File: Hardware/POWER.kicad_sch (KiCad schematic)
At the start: 0 parts

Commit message: Checkpoint
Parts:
- added BT1: Battery_Cell, symbol Device:Battery_Cell
- added U5, U7: AP2112K-3.3, Package_TO_SOT_SMD:SOT-23-5, symbol Regulator_Linear:AP2112K-3.3
- added U6: AP2112K-1.8, Package_TO_SOT_SMD:SOT-23-5, symbol Regulator_Linear:AP2112K-1.8
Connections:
- new net: U5.1 (VIN), U5.3 (EN)
- new net D0_3V3_BACKUP: BT1.1 (+)
- new net D1_3V3: U5.5 (VOUT)
- new net D2_1V8: U6.5 (VOUT)
- new net D2_3V3: U7.5 (VOUT)
- new net GND: BT1.2 (-)
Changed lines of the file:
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@@
 (kicad_sch (version 20230121) (generator eeschema)
   (paper "A4")
+  (wire (pts (xy 50.8 38.1) (xy 53.34 38.1))
+    (stroke (width 0) (type default))
+  )
+  (wire (pts (xy 30.48 170.18) (xy 30.48 172.72))
+    (stroke (width 0) (type default))
+  )
+  (wire (pts (xy 50.8 40.64) (xy 50.8 38.1))
+    (stroke (width 0) (type default))
+  )
+  (wire (pts (xy 53.34 40.64) (xy 50.8 40.64))
+    (stroke (width 0) (type default))
+  )
+  (wire (pts (xy 33.02 170.18) (xy 30.48 170.18))
+    (stroke (width 0) (type default))
+  )
+  (bus (pts (xy 241.3 25.4) (xy 266.7 25.4))
+    (stroke (width 0) (type default))
+  )
+  (label "MEAS_S[1..6]" (at 241.3 25.4 0) (fields_autoplaced)
+    (effects (font (size 1.27 1.27)) (justify left bottom))
+  )
+  (hierarchical_label "SERVO_5V5" (shape input) (at 127 116.84 0) (fields_autoplaced)
+    (effects (font (size 1.27 1.27)) (justify left))
+  )
+  (hierarchical_label "D1_5V" (shape passive) (at 127 104.14 0) (fields_autoplaced)
+    (effects (font (size 1.27 1.27)) (justify left))
+  )
+  (hierarchical_label "D1_3V3" (shape passive) (at 68.58 38.1 0) (fields_autoplaced)
+    (effects (font (size 1.27 1.27)) (justify left))
+  )
+  (hierarchical_label "D2_3V3" (shape passive) (at 170.18 63.5 0) (fields_autoplaced)
+    (effects (font (size 1.27 1.27)) (justify left))
+  )
+  (hierarchical_label "MEAS_S[1..6]" (shape output) (at 266.7 25.4 0) (fields_autoplaced)
+    (effects (font (size 1.27 1.27)) (justify left))
+  )
+  (hierarchical_label "D2_EN" (shape input) (at 152.4 109.22 0) (fields_autoplaced)
+    (effects (font (size 1.27 1.27)) (justify left))
+  )
+  (hierarchical_label "D2_1V8" (shape passive) (at 170.18 33.02 0) (fields_autoplaced)
+    (effects (font (size 1.27 1.27)) (justify left))
+  )
+  (hierarchical_label "D1_EN" (shape input) (at 152.4 106.68 0) (fields_autoplaced)
+    (effects (font (size 1.27 1.27)) (justify left))
+  )
+  (hierarchical_label "MEAS_SERVO" (shape output) (at 152.4 114.3 0) (fields_autoplaced)
+    (effects (font (size 1.27 1.27)) (justify left))
+  )
+  (hierarchical_label "D0_3V3_BACKUP" (shape passive) (at 33.02 170.18 0) (fields_autoplaced)
+    (effects (font (size 1.27 1.27)) (justify left))
+  )
+  (symbol (lib_id "Regulator_Linear:AP2112K-3.3") (at 60.96 40.64 0) (unit 1)
+    (in_bom yes) (on_board yes) (dnp no) (fields_autoplaced)
+    (property "Reference" "U5" (at 60.96 31.75 0)
+      (effects (font (size 1.27 1.27)))
+    )
+    (property "Value" "AP2112K-3.3" (at 60.96 34.29 0)
+      (effects (font (size 1.27 1.27)))
+    )
+    (property "Footprint" "Package_TO_SOT_SMD:SOT-23-5" (at 60.96 32.385 0)
+      (effects (font (size 1.27 1.27)) hide)
+    )
+    (property "Datasheet" "https://www.diodes.com/assets/Datasheets/AP2112.pdf" (at 60.96 38.1 0)
+      (effects (font (size 1.27 1.27)) hide)
+    )
+    (pin "1")
+    (pin "2")
+    (pin "3")
+    (pin "4")
+    (pin "5")
+    (instances
+      (project "Avionus_Flight_Controller"
+        (path "/ddc7e940-0588-4587-8902-8ced9e615ace/26f6db01-be5b-4944-aca8-25d2b5bac430"
+          (reference "U5") (unit 1)
+        )
+      )
+    )
+  )
+  (symbol (lib_id "power:GND") (at 30.48 180.34 0) (unit 1)
+    (in_bom yes) (on_board yes) (dnp no) (fields_autoplaced)
+    (property "Reference" "#PWR012" (at 30.48 186.69 0)
+      (effects (font (size 1.27 1.27)) hide)
+    )
+    (property "Value" "GND" (at 30.48 185.42 0)
+      (effects (font (size 1.27 1.27)))
+    )
+    (property "Footprint" "" (at 30.48 180.34 0)
+      (effects (font (size 1.27 1.27)) hide)
+    )
+    (property "Datasheet" "" (at 30.48 180.34 0)
+      (effects (font (size 1.27 1.27)) hide)
+    )
+    (pin "1")
+    (instances
+      (project "Avionus_Flight_Controller"
+        (path "/ddc7e940-0588-4587-8902-8ced9e615ace/26f6db01-be5b-4944-aca8-25d2b5bac430"
+          (reference "#PWR012") (unit 1)
+        )
+      )
+    )
+  )
+  (symbol (lib_id "Regulator_Linear:AP2112K-3.3") (at 162.56 66.04 0) (unit 1)
+    (in_bom yes) (on_board yes) (dnp no) (fields_autoplaced)
+    (property "Reference" "U7" (at 162.56 57.15 0)
+      (effects (font (size 1.27 1.27)))
+    )
+    (property "Value" "AP2112K-3.3" (at 162.56 59.69 0)
+      (effects (font (size 1.27 1.27)))
+    )
+    (property "Footprint" "Package_TO_SOT_SMD:SOT-23-5" (at 162.56 57.785 0)
+      (effects (font (size 1.27 1.27)) hide)
+    )
+    (property "Datasheet" "https://www.diodes.com/assets/Datasheets/AP2112.pdf" (at 162.56 63.5 0)
+      (effects (font (size 1.27 1.27)) hide)
+    )
+    (pin "1")
+    (pin "2")
+    (pin "3")
+    (pin "4")
+    (pin "5")
+    (instances
+      (project "Avionus_Flight_Controller"
+        (path "/ddc7e940-0588-4587-8902-8ced9e615ace/26f6db01-be5b-4944-aca8-25d2b5bac430"
+          (reference "U7") (unit 1)
+        )
+      )
+    )
+  )
+  (symbol (lib_id "Regulator_Linear:AP2112K-1.8") (at 162.56 35.56 0) (unit 1)
+    (in_bom yes) (on_board yes) (dnp no) (fields_autoplaced)
+    (property "Reference" "U6" (at 162.56 26.67 0)
+      (effects (font (size 1.27 1.27)))
+    )
+    (property "Value" "AP2112K-1.8" (at 162.56 29.21 0)
+      (effects (font (size 1.27 1.27)))
+    )
+    (property "Footprint" "Package_TO_SOT_SMD:SOT-23-5" (at 162.56 27.305 0)
+      (effects (font (size 1.27 1.27)) hide)
+    )
+    (property "Datasheet" "https://www.diodes.com/assets/Datasheets/AP2112.pdf" (at 162.56 33.02 0)
+      (effects (font (size 1.27 1.27)) hide)
+    )
+    (pin "1")
+    (pin "2")
+    (pin "3")
+    (pin "4")
+    (pin "5")
+    (instances
+      (project "Avionus_Flight_Controller"
+        (path "/ddc7e940-0588-4587-8902-8ced9e615ace/26f6db01-be5b-4944-aca8-25d2b5bac430"
+          (reference "U6") (unit 1)
+        )
+      )
+    )
+  )
+  (symbol (lib_id "Device:Battery_Cell") (at 30.48 177.8 0) (unit 1)
+    (in_bom yes) (on_board yes) (dnp no) (fields_autoplaced)
+    (property "Reference" "BT1" (at 34.29 174.6885 0)
+      (effects (font (size 1.27 1.27)) (justify left))
+    )
+    (property "Value" "Battery_Cell" (at 34.29 177.2285 0)
+      (effects (font (size 1.27 1.27)) (justify left))
+    )
+    (property "Footprint" "" (at 30.48 176.276 90)
+      (effects (font (size 1.27 1.27)) hide)
+    )
+    (property "Datasheet" "~" (at 30.48 176.276 90)
+      (effects (font (size 1.27 1.27)) hide)
+    )
+    (pin "1")
+    (pin "2")
+    (instances
+      (project "Avionus_Flight_Controller"
+        (path "/ddc7e940-0588-4587-8902-8ced9e615ace/26f6db01-be5b-4944-aca8-25d2b5bac430"
+          (reference "BT1") (unit 1)
+        )
+      )
+    )
+  )
 )

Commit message: Checkpoint
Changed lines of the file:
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@@
+    (effects (font (size 1.27 1.27)) (justify left))
+  )
+  (hierarchical_label "USB_5V" (shape input) (at 127 119.38 0) (fields_autoplaced)
     (effects (font (size 1.27 1.27)) (justify left))
   )

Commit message: Checkpoint
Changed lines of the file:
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@@
+    (effects (font (size 1.27 1.27)) (justify left))
+  )
+  (hierarchical_label "POWER_LED_EN" (shape input) (at 152.4 116.84 0) (fields_autoplaced)
     (effects (font (size 1.27 1.27)) (justify left))
   )

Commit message: Checkpoint
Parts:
- added C13, C14, C15, C16, C17, C18: 1uF, symbol Device:C_Small
- added C15: 120uF, Capacitor_THT:C_Radial_D6.3mm_H11.0mm_P2.50mm, symbol Device:C
- added C19, C20, C21, C22: 100nF, symbol Device:C_Small
- added C30, C39: 22uF, Capacitor_SMD:C_1210_3225Metric, symbol Device:C
- added C31: 1uF, Capacitor_SMD:C_0805_2012Metric, symbol Device:C
- added C33: 100pF, Capacitor_SMD:C_0805_2012Metric, symbol Device:C
- added C34: 100nF, Capacitor_SMD:C_0805_2012Metric, symbol Device:C
- added D1, D2, D3: ~, symbol Device:LED_Small
- added D13: B540C-13-F, Diode_SMD:D_SMC, symbol Device:D_Schottky
- added F1: 2000mA, Fuse:Fuse_1206_3216Metric, symbol Device:Polyfuse
- added J15: 5V_USB, symbol Connector_Generic:Conn_01x02
- added J17: Battery IN, symbol Connector_Generic:Conn_01x07
- added L1: SRP6530A-6R8M, leptunKicadLib:SRP6530A-6R8M, symbol Device:L
- added Q1: RE1C002UN, Package_TO_SOT_SMD:SOT-416, symbol Device:Q_NMOS_GSD
- added R25: 15K, Resistor_SMD:R_1206_3216Metric, symbol Device:R
- added R28: 52.3K, Resistor_SMD:R_1206_3216Metric, symbol Device:R_Small
- added R29: 10K, Resistor_SMD:R_1206_3216Metric, symbol Device:R_Small
- added R32: 100, symbol Device:R_Small
- added R33, R40, R41, R42, R46, R47, R48, R49, R50, R51, R52: 100K, symbol Device:R_Small
- added R34, R38, R39: 1K, symbol Device:R_Small
- added R53, R54, R55, R56, R57, R58, R59: 10K, symbol Device:R_Small
- added TP2, TP3, TP4, TP5, TP6, TP7: ~, symbol Connector:TestPoint
- added U11: AOZ1212AI, leptunKicadLib:AOZ1212AI, symbol leptunKicadLib:AOZ1212AI
- added U5 (x2): AP2151W, Package_TO_SOT_SMD:SOT-23-5, symbol leptunKicadLib:AP2151W
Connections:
- net D0_3V3_BACKUP: now also TP2.1
- net D1_3V3: now also C14.1
- net D1_5V: now also U5.1 (VIN), U5.3 (EN), U6.1 (VIN), U7.1 (VIN), C13.1, C15.1, C17.1, C19.1, C20.1, C39.2, J15.2 (Pin_2), L1.2, R28.1, TP3.1, U5.5 (IN), U5.5 (IN)
- net D1_EN: now also R34.1, R40.2, U11.6 (EN)
- net D2_1V8: now also C16.1, TP5.1
- net D2_3V3: now also C18.1, TP4.1
- net D2_EN: now also U6.3 (EN), U7.3 (EN), R38.1, R41.1
- net GND: now also U5.2 (GND), U6.2 (GND), U7.2 (GND), C13.2, C14.2, C15.2, C15.2, C16.2, C17.2, C18.2, C19.2, C20.2, C21.2, C22.2, C30.1, C31.1, C33.1, C39.1, D13.2 (A), J17.1 (Pin_1), Q1.2 (S), R29.2, R33.2, R40.1, R41.2, R42.2, R53.2, R54.2, R55.2, R56.2, R57.2, R58.2, R59.2, U11.3 (GND), U5.2 (GND), U5.2 (GND)
- net MEAS_SERVO: now also R52.2, R53.1
- net SERVO_5V5: now also C15.1, C21.1, C22.1, R52.1, TP7.1, U5.1 (OUT), U5.1 (OUT)
- net USB_5V: now also J15.1 (Pin_1), TP6.1
- new net: D1.1 (K), D2.1 (K), D3.1 (K), Q1.3 (D)
- new net: D3.2 (A), R39.2
- new net: Q1.1 (G), R32.2
- new net: D2.2 (A), R38.2
- new net: C33.2, R25.1
- new net: R25.2, U11.5 (COMP)
- new net: R28.2, R29.1, U11.4 (FB)
- new net: D1.2 (A), R34.2
- new net: C31.2, U11.8 (VBIAS)
- new net: C34.2, D13.1 (K), L1.1, U11.1 (LX)
- new net: C34.1, U11.2 (BST)
- new net: C30.2, F1.1, U11.7 (VIN)
- new net BATT_S1: J17.2 (Pin_2), R51.2
- new net BATT_S2: J17.3 (Pin_3), R50.1
- new net BATT_S3: J17.4 (Pin_4), R49.1
- new net BATT_S4: J17.5 (Pin_5), R48.1
- new net BATT_S5: J17.6 (Pin_6), R47.1
- new net BATT_S6: F1.2, J17.7 (Pin_7), R46.1
- new net LEDs_EN: R32.1, R33.1
- new net MEAS_S1: R51.1, R59.1
- new net MEAS_S2: R50.2, R58.1
- new net MEAS_S3: R49.2, R57.1
- new net MEAS_S4: R48.2, R56.1
- new net MEAS_S5: R47.2, R55.1
- new net MEAS_S6: R46.2, R54.1
- new net SERVO_5V_AUX_EN: R39.1, R42.1, U5.4 (EN), U5.4 (EN)
- new net SERVO_5V_AUX_FAULT: U5.3 (~{FLG}), U5.3 (~{FLG})
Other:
- moved on the sheet: BT1, U5, U6, U7

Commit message: Checkpoint
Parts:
- added C48: 4.7uF, symbol Device:C_Small
- added D5: BAT54C, Package_TO_SOT_SMD:SOT-23, symbol Diode:BAT54C
- C33, C34: footprint Capacitor_SMD:C_0805_2012Metric -> (none)
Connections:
- net D1_EN: now also D5.1; no longer R40.2, U11.6 (EN)
- net GND: now also R40.2, C48.2; no longer R40.1
- net at C30.2, F1.1, U11.7 (VIN): now also D5.2
- new net: C48.1, D5.3, R40.1, U11.6 (EN)
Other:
- moved on the sheet: C30, C31, C33, C34, C39, D13, F1, L1, R25, R28, R29, R40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

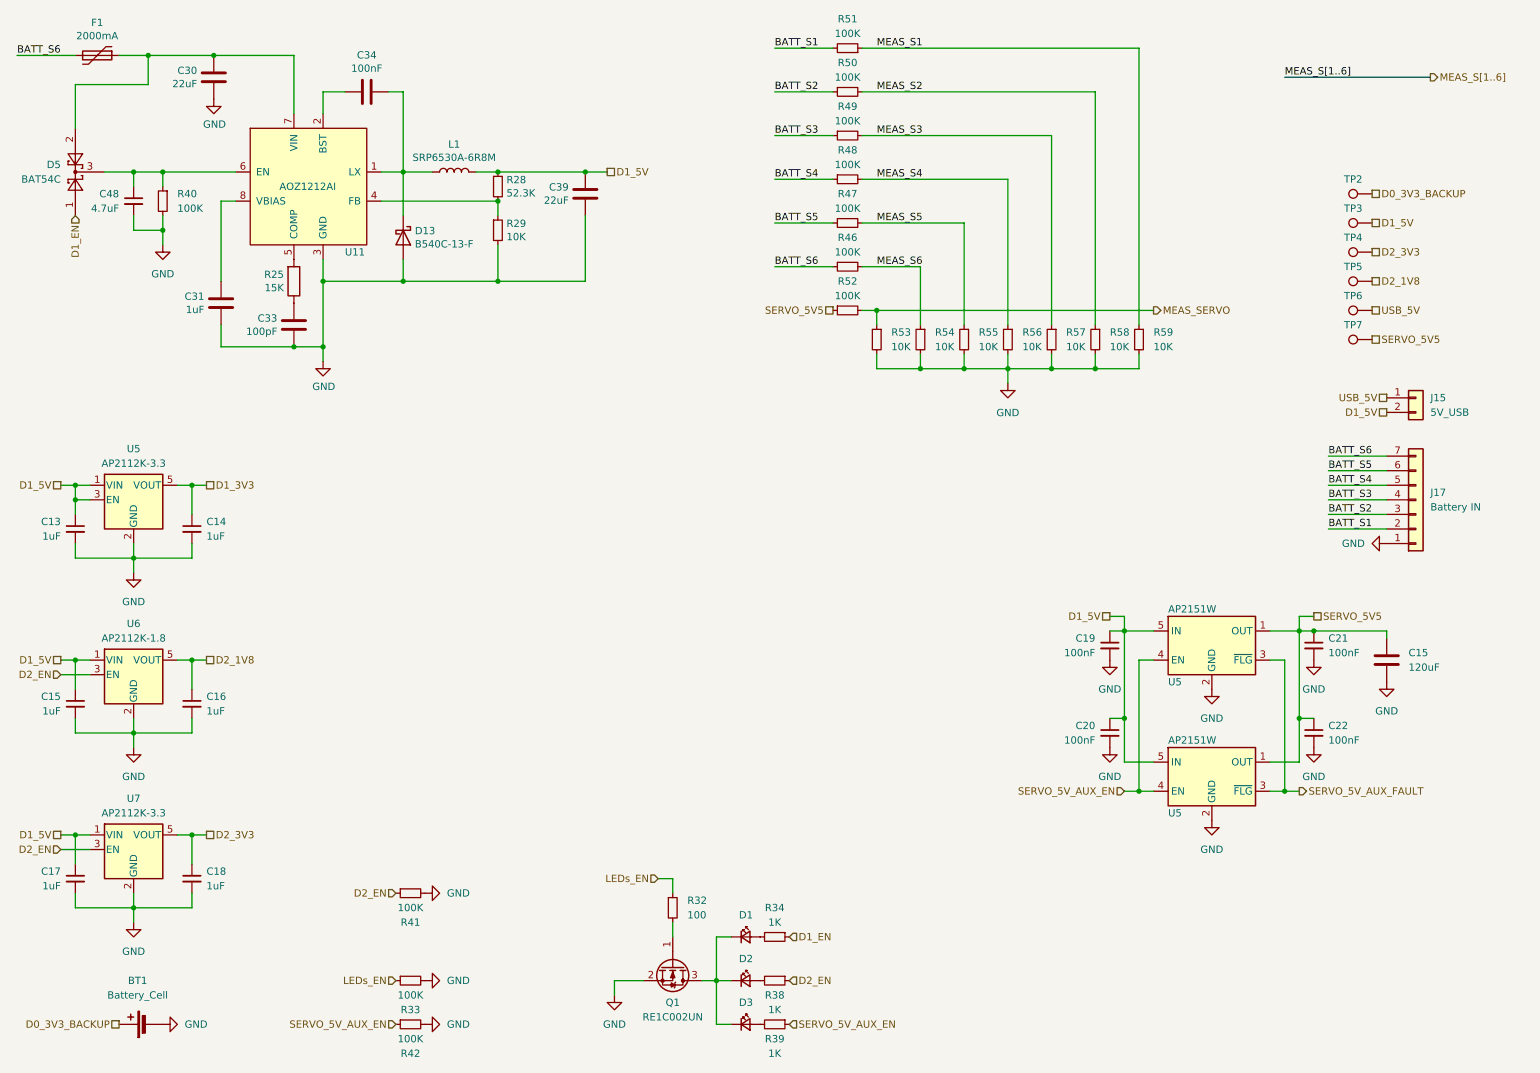
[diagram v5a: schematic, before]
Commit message: ERC fixes
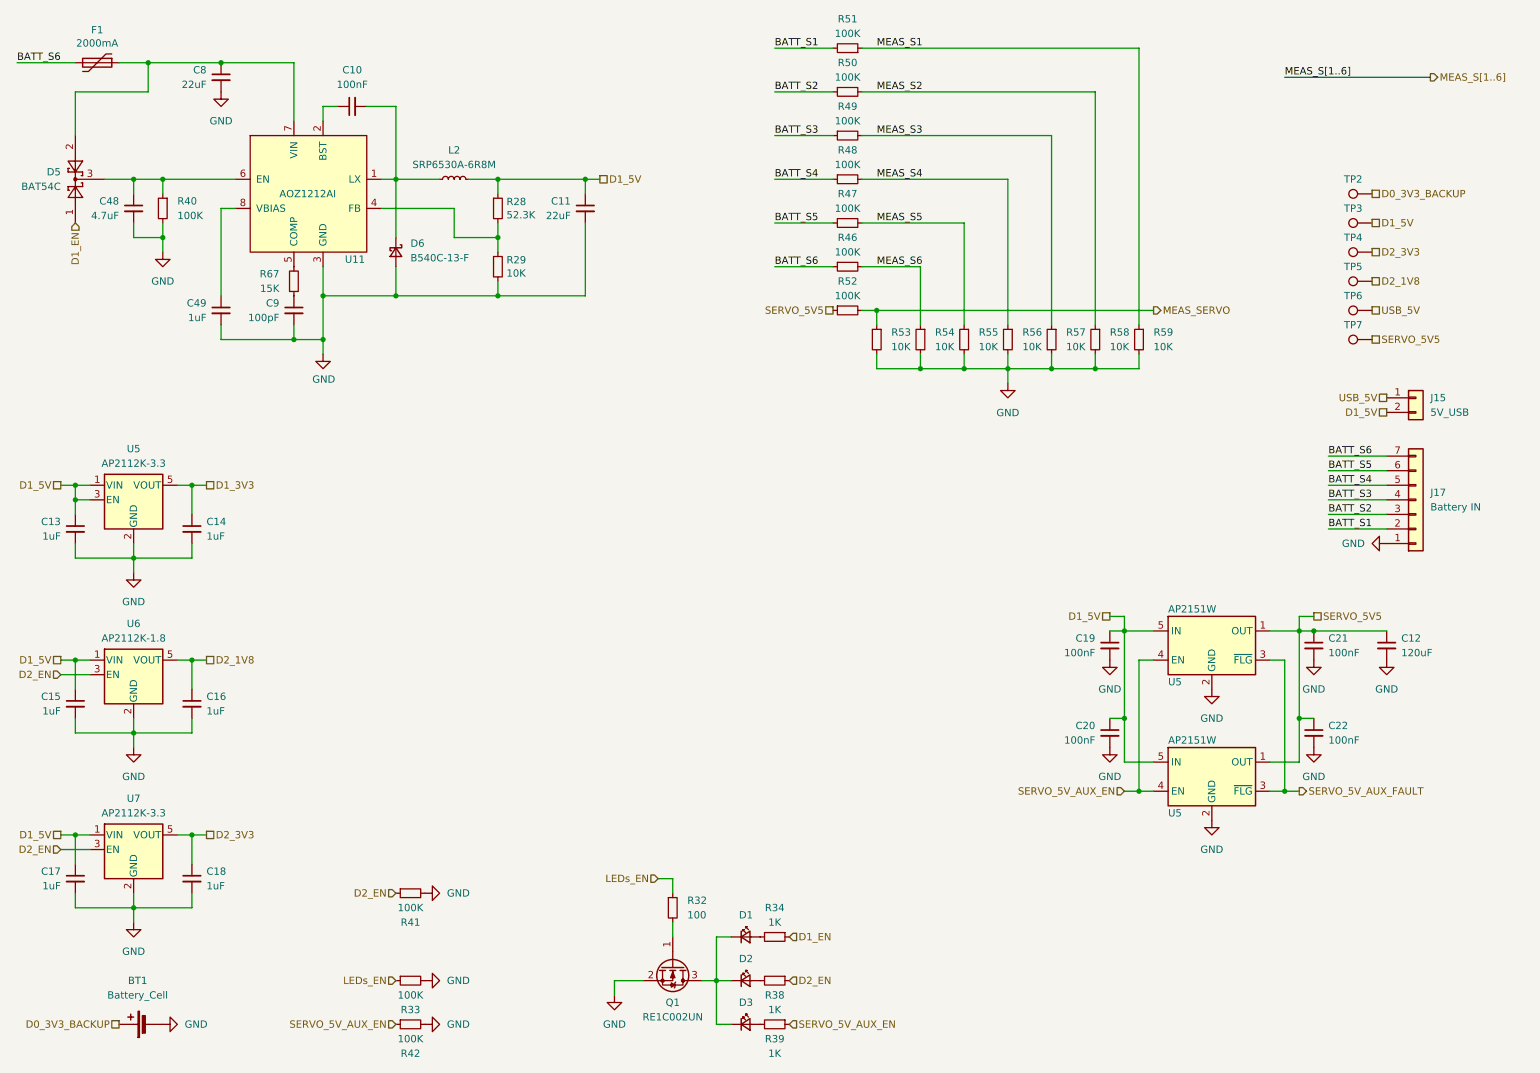
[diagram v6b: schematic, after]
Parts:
- removed C15: 120uF, Capacitor_THT:C_Radial_D6.3mm_H11.0mm_P2.50mm, symbol Device:C
- removed C30, C39: 22uF, Capacitor_SMD:C_1210_3225Metric, symbol Device:C
- removed C31: 1uF, Capacitor_SMD:C_0805_2012Metric, symbol Device:C
- removed C33: 100pF, symbol Device:C
- removed C34: 100nF, symbol Device:C
- removed D13: B540C-13-F, Diode_SMD:D_SMC, symbol Device:D_Schottky
- removed L1: SRP6530A-6R8M, leptunKicadLib:SRP6530A-6R8M, symbol Device:L
- removed R25: 15K, Resistor_SMD:R_1206_3216Metric, symbol Device:R
- added C10: 100nF, symbol Device:C_Small
- added C11, C8: 22uF, Capacitor_SMD:C_1210_3225Metric, symbol Device:C_Small
- added C12: 120uF, Capacitor_THT:C_Radial_D6.3mm_H11.0mm_P2.50mm, symbol Device:C_Small
- added C49: 1uF, symbol Device:C_Small
- added C9: 100pF, symbol Device:C_Small
- added D6: B540C-13-F, Diode_SMD:D_SMC, symbol Device:D_Schottky_Small
- added L2: SRP6530A-6R8M, leptunKicadLib:SRP6530A-6R8M, symbol Device:L_Small
- added R67: 15K, symbol Device:R_Small
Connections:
- net D1_5V: now also C11.1, L2.2
- net GND: now also C11.2, C12.2, C49.2, C8.2, C9.2, D6.2 (A)
- net SERVO_5V5: now also C12.1
- net at U11.5 (COMP): now also R67.2
- net at U11.8 (VBIAS): now also C49.1
- net at U11.1 (LX): now also C10.2, D6.1 (K), L2.1
- net at U11.2 (BST): now also C10.1
- net at D5.2, F1.1, U11.7 (VIN): now also C8.1
- new net: C9.1, R67.1
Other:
- moved on the sheet: C48, D5, F1, R28, R29, R40, U11

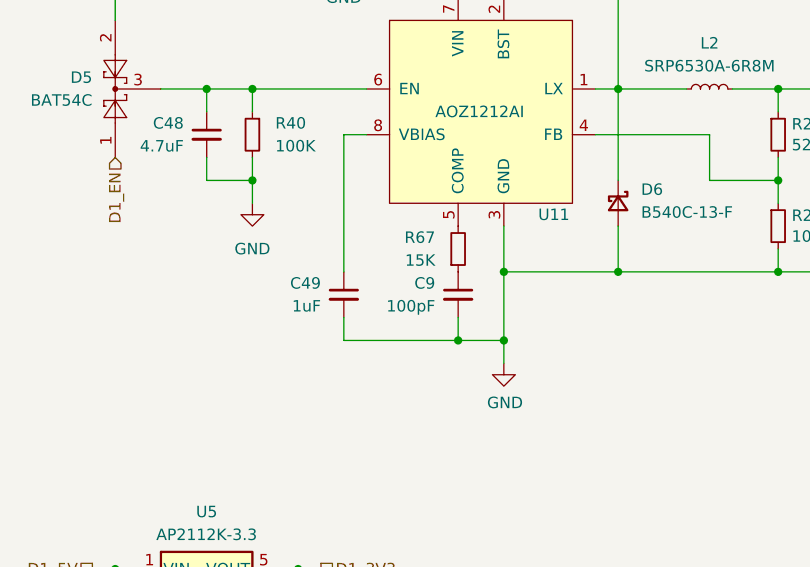
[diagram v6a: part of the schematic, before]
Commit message: Update Buck converter compensation circuitry
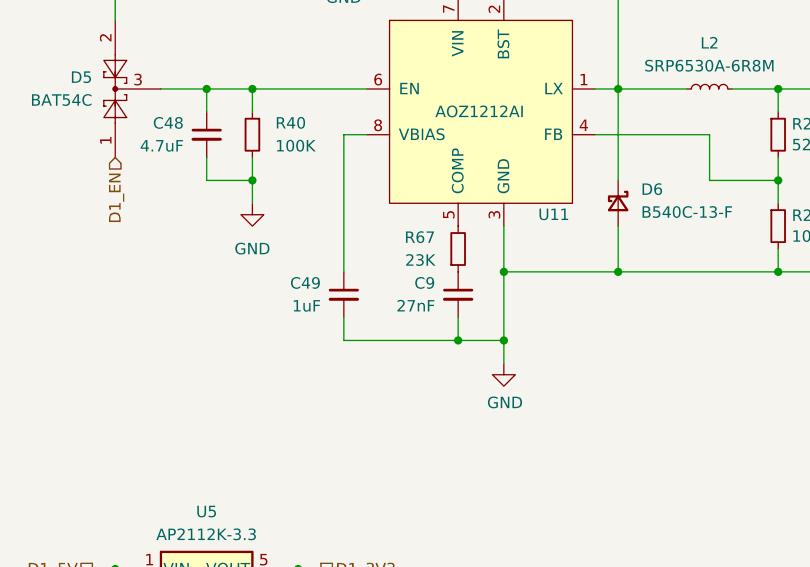
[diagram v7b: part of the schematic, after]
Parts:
- C9: value 100pF -> 27nF
- R67: value 15K -> 23K
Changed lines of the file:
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@@
       (effects (font (size 1.27 1.27)) (justify right))
     )
-    (property "Value" "15K" (at 66.04 62.23 0)
+    (property "Value" "23K" (at 66.04 62.23 0)
       (effects (font (size 1.27 1.27)) (justify right))
     )
@@
       (effects (font (size 1.27 1.27)) (justify left))
     )
-    (property "Value" "100pF" (at 66.04 67.3163 0)
-      (effects (font (size 1.27 1.27)) (justify left))
-    )
+    (property "Value" "27nF" (at 66.04 67.3163 0)
+      (effects (font (size 1.27 1.27)) (justify left))
+    )
